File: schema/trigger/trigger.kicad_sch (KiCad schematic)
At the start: 16 parts, among them J1 Barrel_Jack, J2 Conn_01x02_Socket, Q1 DMG4800LK3-13

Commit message: mcu
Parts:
- added C8: 100n, Capacitor_SMD:C_0603_1608Metric, symbol Device:C_Small
- added IC1: RP2040_ZERO, symbol mySymbols:RP2040_ZERO
- added J3: Conn_01x02_Pin, symbol Connector:Conn_01x02_Pin
- added R6: 1k0, Resistor_SMD:R_0603_1608Metric, symbol Device:R_Small
- added R7: 4k7, Resistor_SMD:R_0603_1608Metric, symbol Device:R_Small
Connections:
- net GND: now also C8.2, IC1.2 (GND), J3.2 (Pin_2)
- net TRIGGER: now also IC1.8 (15)
- net VSENSE: now also IC1.7 (26)
- new net: J3.1 (Pin_1), R6.2
- new net +3V3: IC1.3 (3V3), R7.1
- new net +5V: IC1.1 (5V)
- new net LOCKED: C8.1, IC1.9 (14), R6.1, R7.2

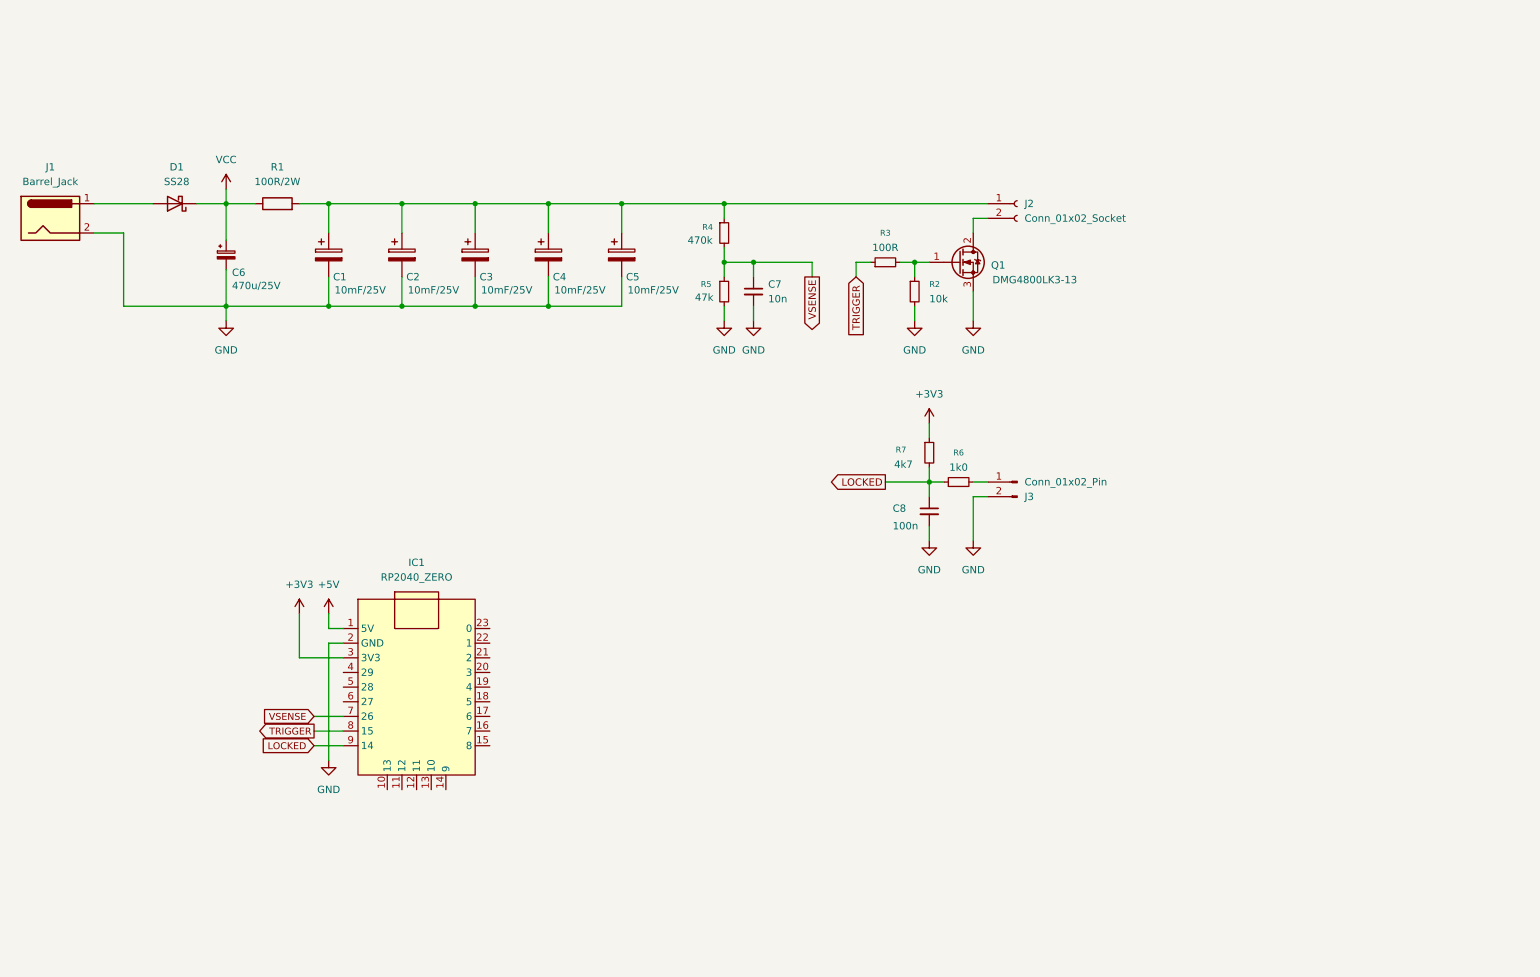
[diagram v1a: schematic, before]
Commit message: led to blink, otherwise it'll never work
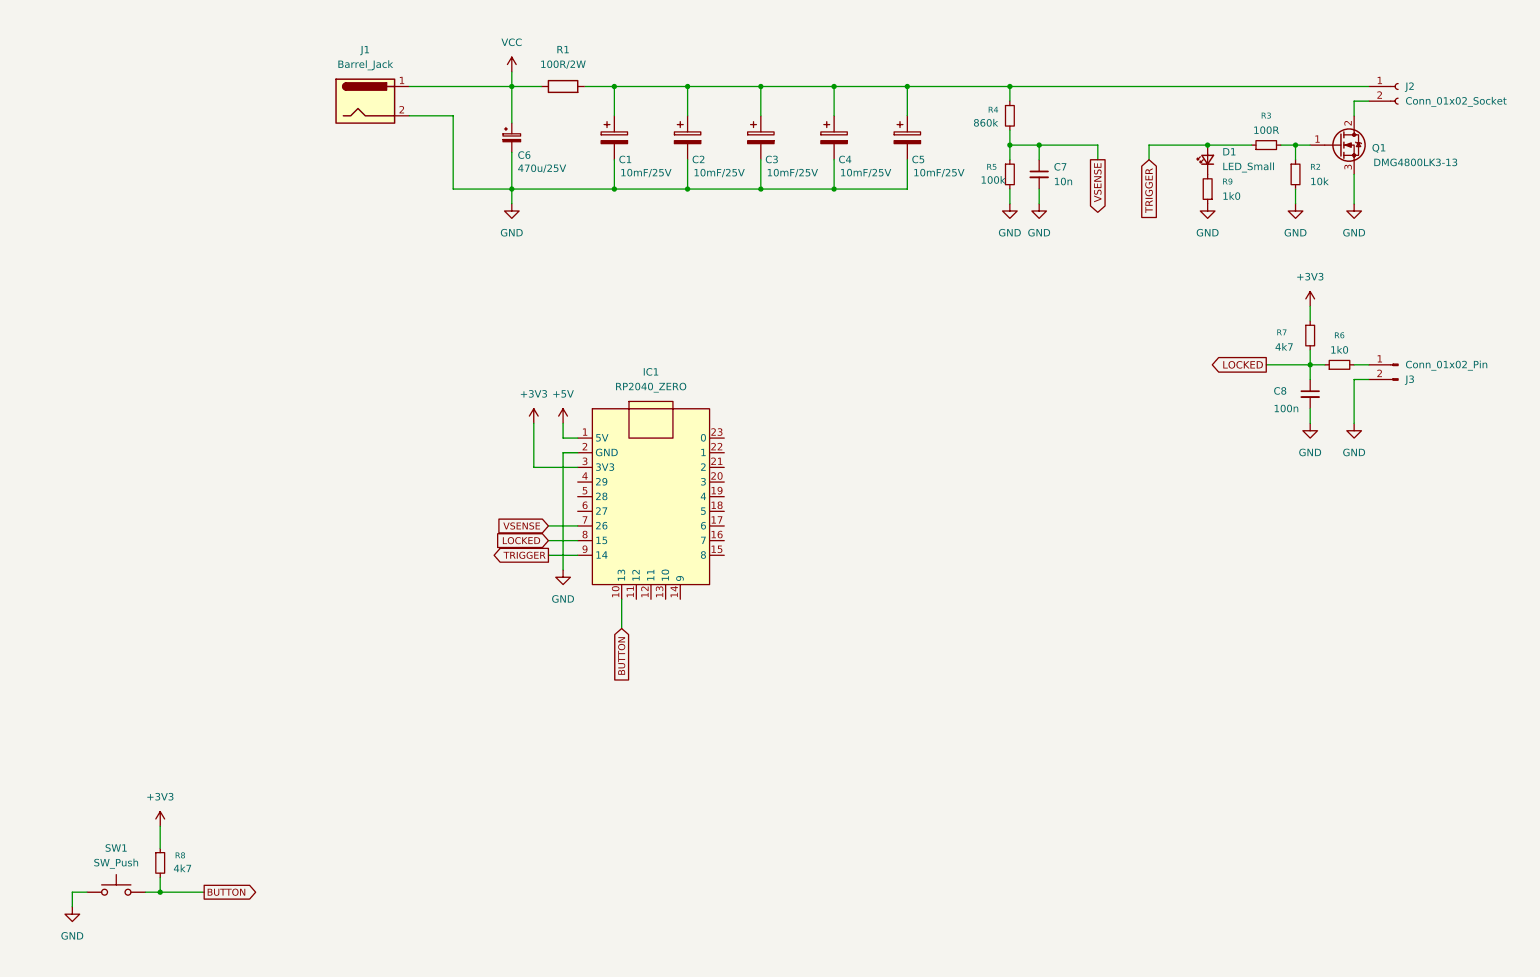
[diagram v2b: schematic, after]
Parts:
- removed D1: SS28, Diode_SMD:D_SMB, symbol Device:D_Schottky
- added D1: LED_Small, symbol Device:LED_Small
- added R8: 4k7, Resistor_SMD:R_0603_1608Metric, symbol Device:R_Small
- added R9: 1k0, Resistor_SMD:R_0603_1608Metric, symbol Device:R_Small
- added SW1: SW_Push, symbol Switch:SW_Push
- R4: value 470k -> 860k
- R5: value 47k -> 100k
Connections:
- net +3V3: now also R8.1
- net GND: now also R9.1, SW1.1
- net LOCKED: now also IC1.8 (15); no longer IC1.9 (14)
- net TRIGGER: now also IC1.9 (14), D1.2 (A); no longer IC1.8 (15)
- net VCC: now also J1.1
- net BUTTON: now reaches IC1.10 (13)
- net BUTTON: now also R8.2, SW1.2
- new net: D1.1 (K), R9.2
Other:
- moved on the sheet: C1, C2, C3, C4, C5, C6, C7, C8, IC1, J1, J2, J3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

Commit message: non specified schematic changes (led, maybe?)
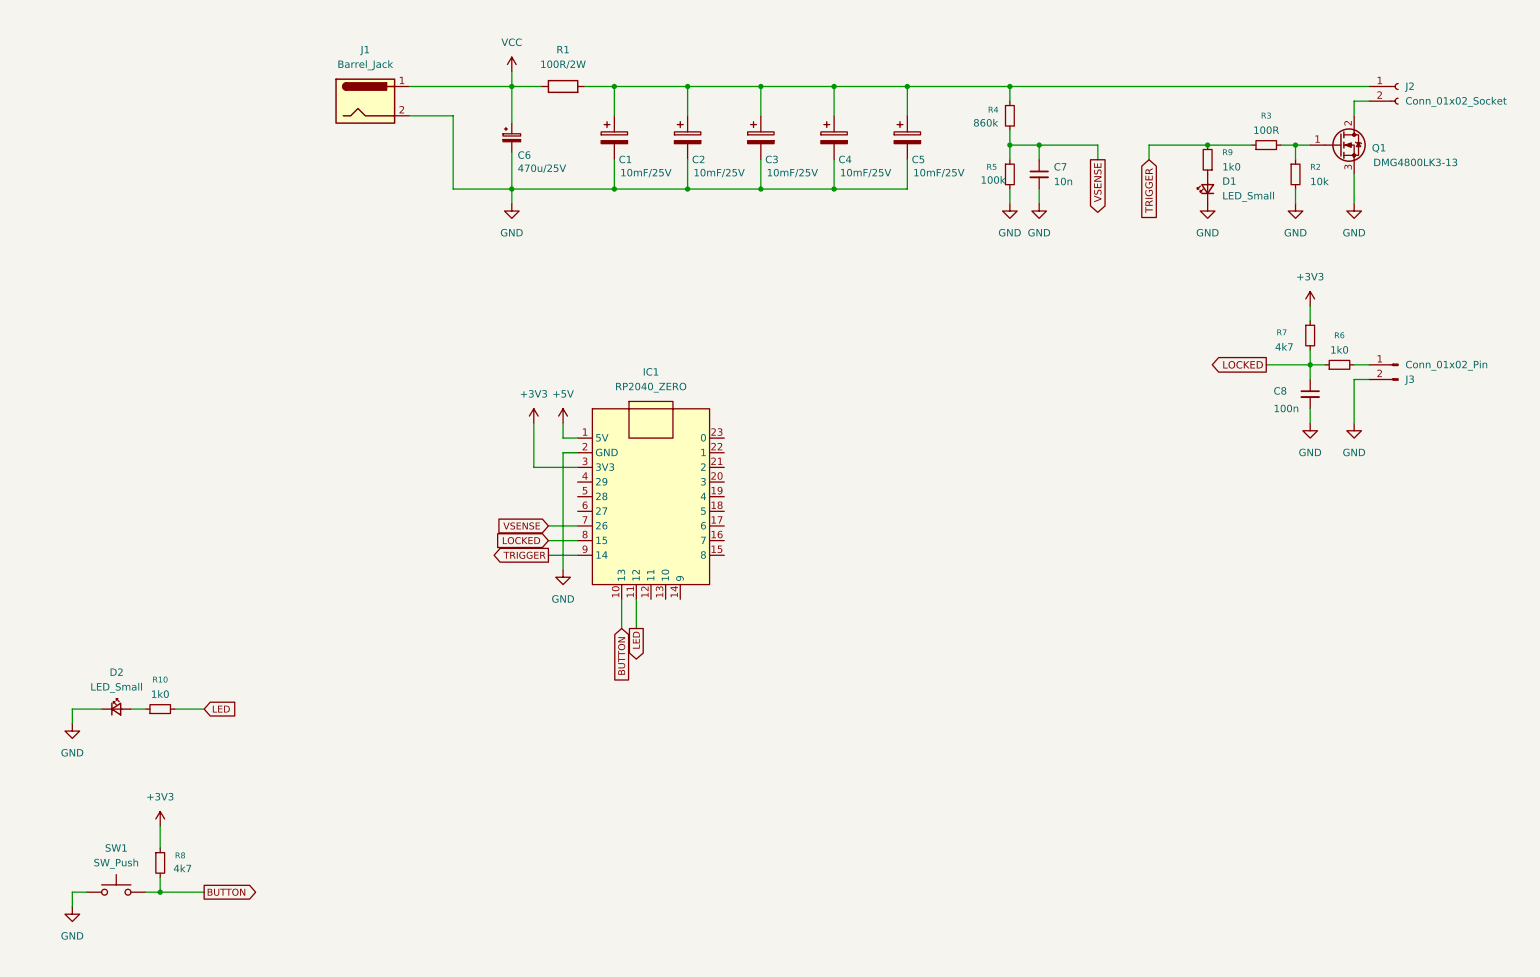
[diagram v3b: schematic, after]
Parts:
- added D2: LED_Small, symbol Device:LED_Small
- added R10: 1k0, Resistor_SMD:R_0603_1608Metric, symbol Device:R_Small
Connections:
- net GND: now also D1.1 (K), D2.1 (K); no longer R9.1
- net TRIGGER: now also R9.2; no longer D1.2 (A)
- net LED: now reaches IC1.11 (12)
- net LED: now also R10.2
- new net: D2.2 (A), R10.1
- new net: D1.2 (A), R9.1
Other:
- moved on the sheet: D1, R9

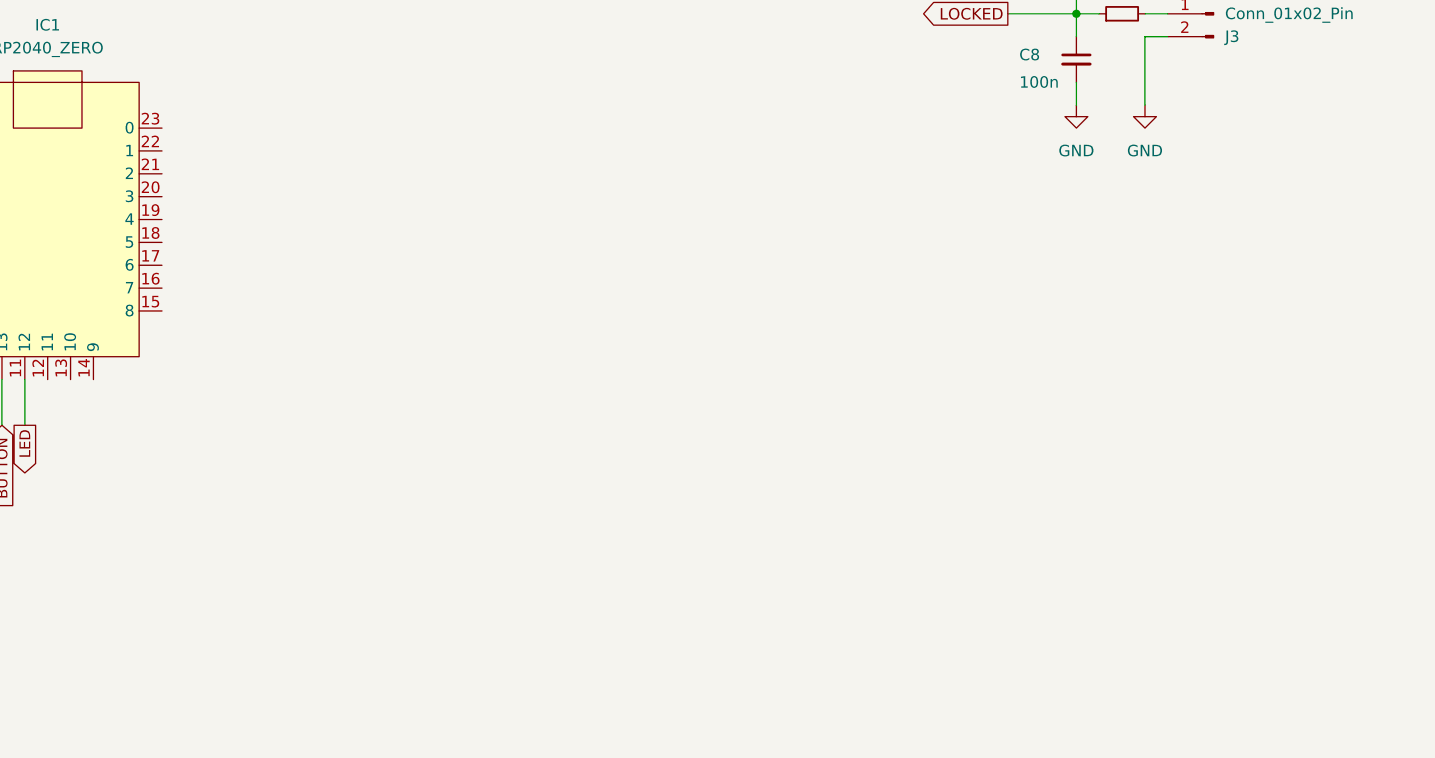
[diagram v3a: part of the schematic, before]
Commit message: display and rtc module
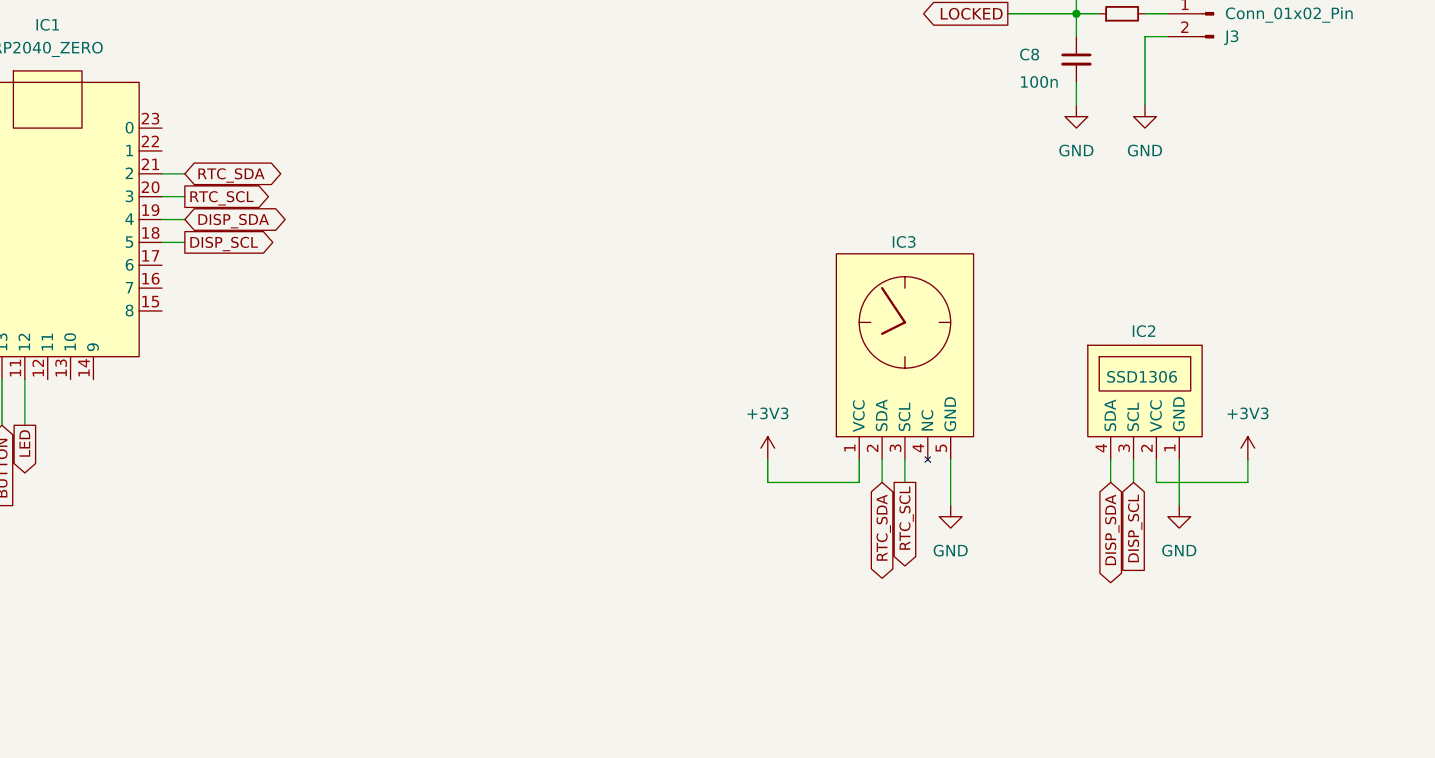
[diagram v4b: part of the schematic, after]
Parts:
- added IC2: SSD1306, symbol mySymbols:OLED_I2C
- added IC3: ~, symbol mySymbols:RTC
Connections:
- net +3V3: now also IC2.2 (VCC), IC3.1 (VCC)
- net GND: now also IC2.1 (GND), IC3.5 (GND)
- net DISP_SCL: now reaches IC1.18 (5)
- net DISP_SCL: now also IC2.3 (SCL)
- net DISP_SDA: now reaches IC1.19 (4)
- net DISP_SDA: now also IC2.4 (SDA)
- net RTC_SCL: now reaches IC1.20 (3)
- net RTC_SCL: now also IC3.3 (SCL)
- net RTC_SDA: now reaches IC1.21 (2)
- net RTC_SDA: now also IC3.2 (SDA)

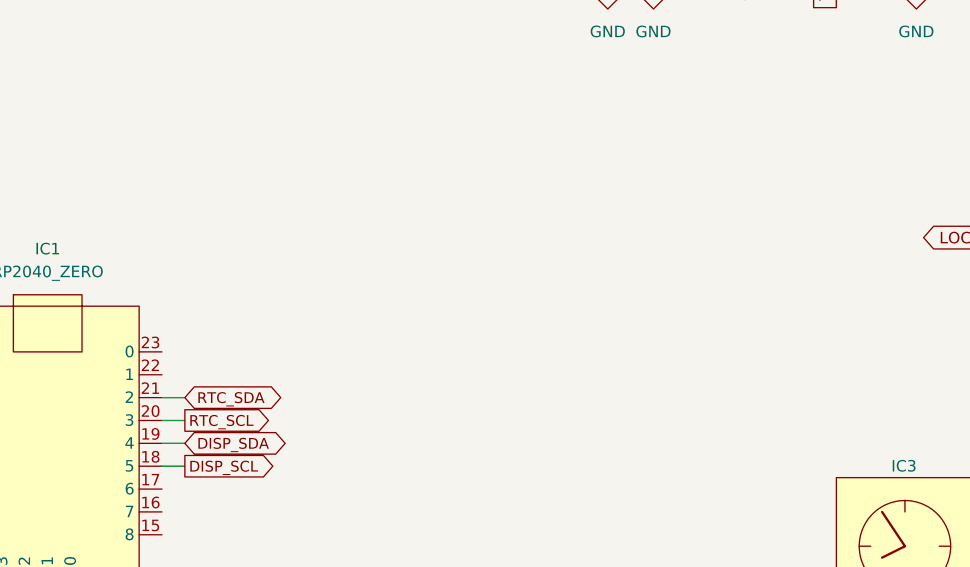
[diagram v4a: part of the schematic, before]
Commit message: schematic - uart connection (radio)
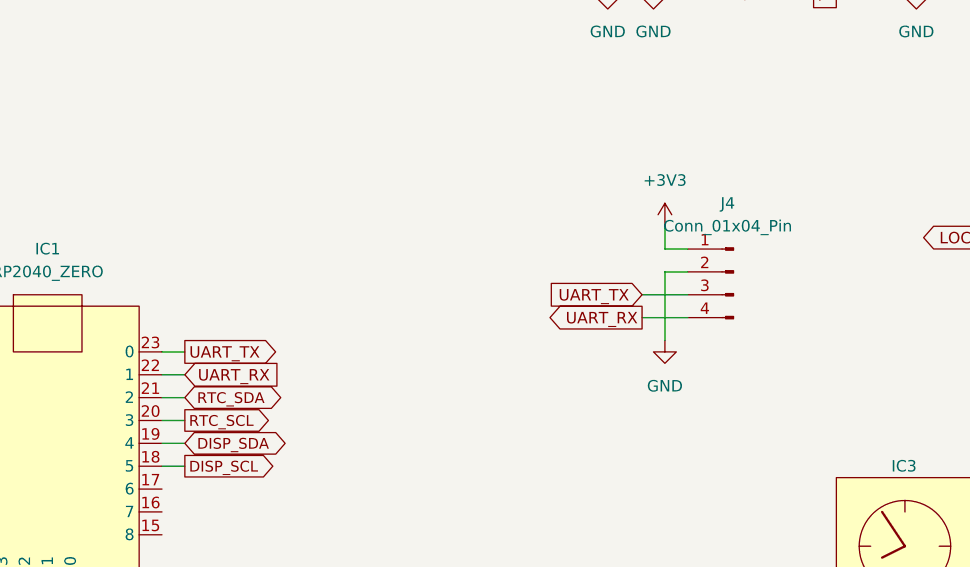
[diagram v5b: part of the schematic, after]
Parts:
- added J4: Conn_01x04_Pin, symbol Connector:Conn_01x04_Pin
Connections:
- net +3V3: now also J4.1 (Pin_1)
- net GND: now also J4.2 (Pin_2)
- net UART_RX: now reaches IC1.22 (1)
- net UART_RX: now also J4.4 (Pin_4)
- net UART_TX: now reaches IC1.23 (0)
- net UART_TX: now also J4.3 (Pin_3)

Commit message: some new packages
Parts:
- removed C5: 10mF/25V, Capacitor_THT:CP_Radial_D18.0mm_P7.50mm, symbol Device:C_Polarized
- C1, C2, C3, C4: footprint Capacitor_THT:CP_Radial_D18.0mm_P7.50mm -> myLibrary:C_36x18
- D1, D2: footprint (none) -> LED_SMD:LED_0805_2012Metric
- IC2: footprint (none) -> myLibrary:OLED_I2C_128x64_THT
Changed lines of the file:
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@@
 	)
 	(junction
-		(at 163.83 55.88)
-		(diameter 0)
-		(color 0 0 0 0)
-	)
-	(junction
 		(at 151.13 55.88)
 		(diameter 0)
@@
 	)
 	(junction
-		(at 176.53 38.1)
-		(diameter 0)
-		(color 0 0 0 0)
-	)
-	(junction
 		(at 246.38 86.36)
 		(diameter 0)
@@
 	(wire
 		(pts
-			(xy 176.53 43.18) (xy 176.53 38.1)
-		)
-		(stroke
-			(width 0)
-			(type default)
-		)
-	)
-	(wire
-		(pts
 			(xy 144.78 99.06) (xy 147.32 99.06)
 		)
@@
 	(wire
 		(pts
-			(xy 176.53 38.1) (xy 163.83 38.1)
+			(xy 163.83 38.1) (xy 194.31 38.1)
 		)
 		(stroke
@@
 	(wire
 		(pts
-			(xy 176.53 38.1) (xy 194.31 38.1)
-		)
-		(stroke
-			(width 0)
-			(type default)
-		)
-	)
-	(wire
-		(pts
 			(xy 119.38 99.06) (xy 116.84 99.06)
 		)
@@
 	(wire
 		(pts
-			(xy 176.53 50.8) (xy 176.53 55.88)
-		)
-		(stroke
-			(width 0)
-			(type default)
-		)
-	)
-	(wire
-		(pts
 			(xy 34.29 177.8) (xy 31.75 177.8)
 		)
@@
 	(wire
 		(pts
-			(xy 176.53 55.88) (xy 163.83 55.88)
-		)
-		(stroke
-			(width 0)
-			(type default)
-		)
-	)
-	(wire
-		(pts
 			(xy 125.73 55.88) (xy 125.73 50.8)
 		)
@@
 			)
 		)
-		(property "Footprint" ""
+		(property "Footprint" "LED_SMD:LED_0805_2012Metric"
 			(at 39.37 146.05 90)
 			(effects
@@
 			)
 		)
-		(property "Footprint" "Capacitor_THT:CP_Radial_D18.0mm_P7.50mm"
+		(property "Footprint" "myLibrary:C_36x18"
 			(at 126.6952 50.8 0)
 			(effects
@@
 			)
 		)
-		(property "Footprint" "Capacitor_THT:CP_Radial_D18.0mm_P7.50mm"
+		(property "Footprint" "myLibrary:C_36x18"
 			(at 139.3952 50.8 0)
 			(effects
@@
 			)
 		)
-		(property "Footprint" "Capacitor_THT:CP_Radial_D18.0mm_P7.50mm"
+		(property "Footprint" "myLibrary:C_36x18"
 			(at 164.7952 50.8 0)
 			(effects
@@
 			)
 		)
-		(property "Footprint" ""
+		(property "Footprint" "myLibrary:OLED_I2C_128x64_THT"
 			(at 254 128.27 0)
 			(effects
@@
 			)
 		)
-		(property "Footprint" ""
+		(property "Footprint" "LED_SMD:LED_0805_2012Metric"
 			(at 228.6 55.88 90)
 			(effects
@@
 			)
 		)
-		(property "Footprint" "Capacitor_THT:CP_Radial_D18.0mm_P7.50mm"
+		(property "Footprint" "myLibrary:C_36x18"
 			(at 152.0952 50.8 0)
 			(effects
@@
 					(unit 1)
 				)
-			)
-		)
-	)
-	(symbol
-		(lib_id "Device:C_Polarized")
-		(at 176.53 46.99 0)
-		(unit 1)
-		(exclude_from_sim no)
-		(in_bom yes)
-		(on_board yes)
-		(dnp no)
-		(property "Reference" "C5"
-			(at 177.292 50.8 0)
-			(effects
-				(font
-					(size 1.27 1.27)
-				)
-				(justify left)
-			)
-		)
-		(property "Value" "10mF/25V"
-			(at 177.546 53.086 0)
-			(effects
-				(font
-					(size 1.27 1.27)
-				)
-				(justify left)
-			)
-		)
-		(property "Footprint" "Capacitor_THT:CP_Radial_D18.0mm_P7.50mm"
-			(at 177.4952 50.8 0)
-			(effects
-				(font
-					(size 1.27 1.27)
-				)
-				(hide yes)
-			)
-		)
-		(property "Datasheet" "~"
-			(at 176.53 46.99 0)
-			(effects
-				(font
-					(size 1.27 1.27)
-				)
-				(hide yes)
-			)
-		)
-		(property "Description" "Polarized capacitor"
-			(at 176.53 46.99 0)
-			(effects
-				(font
-					(size 1.27 1.27)
-				)
-				(hide yes)
-			)
-		)
-		(pin "2"
-		)
-		(pin "1"
-		)
-		(instances
-			(project "trigger"
-				(path "/9d6aa6a3-975e-4ebc-88ff-e01204bd60d9"
-					(reference "C5")
-					(unit 1)
-				)

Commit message: yet another oled footprint
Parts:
- IC2: footprint myLibrary:OLED_I2C_128x64_THT -> myLibrary:OLED_I2C_128x64_SMD
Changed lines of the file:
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@@
 			)
 		)
-		(property "Footprint" "myLibrary:OLED_I2C_128x64_THT"
+		(property "Footprint" "myLibrary:OLED_I2C_128x64_SMD"
 			(at 254 128.27 0)
 			(effects
